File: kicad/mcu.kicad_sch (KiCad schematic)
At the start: 19 parts, among them J301 TC2030-MCP-NL, J302 PinHeader_01x05, U301 STM32F030C8Tx, U302 SRV05-4, Y301 16Mhz

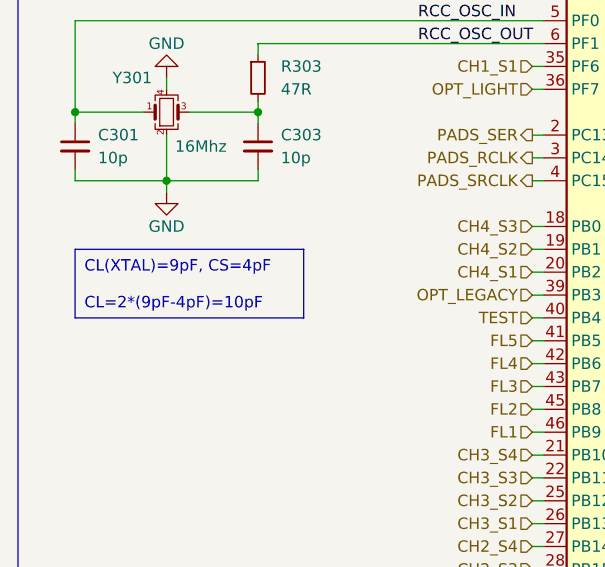
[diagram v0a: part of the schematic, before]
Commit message: fab: update BOM with missing component codes
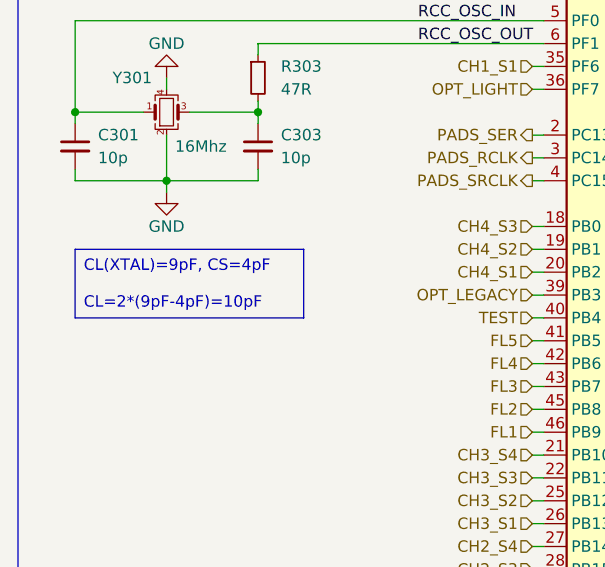
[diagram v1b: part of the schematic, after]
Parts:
- J302: JLCPCB Part # (none) -> C6332198
